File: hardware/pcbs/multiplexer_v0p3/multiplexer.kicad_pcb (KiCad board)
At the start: 2 copper layers, 82.6 x 88.9 mm, 22 parts, among them K1 CONN_3, M1 VAL**, M2 VAL**, M3 VAL**, P1 CONN_5X2, P2 CONN_5X2, P3 CONN_2, P4 CONN_2, P5 CONN_5X2, U1 ADG44X, U2 ADG44X, U3 ADG44X, U4 ADG44X

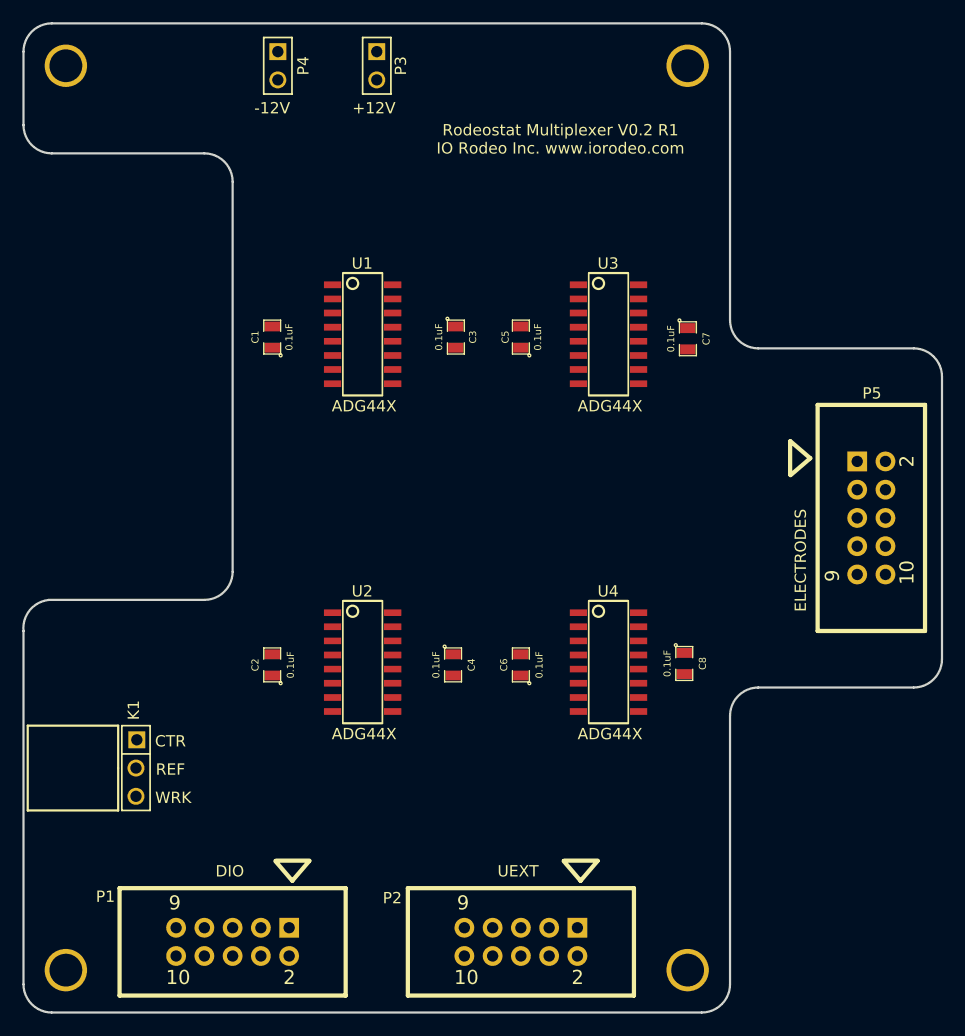
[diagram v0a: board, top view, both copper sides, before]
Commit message: Worked on layout of v0.3 multiplexer design.
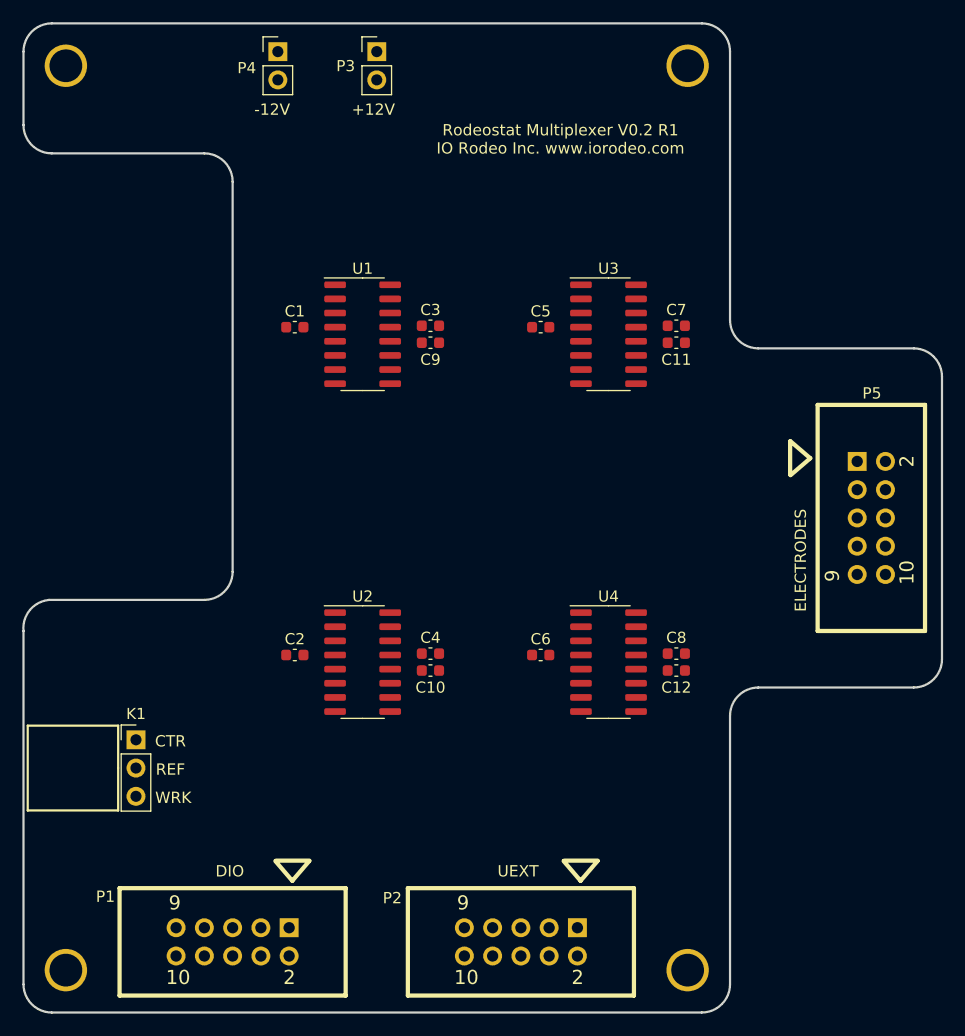
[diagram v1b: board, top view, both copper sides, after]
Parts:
- added C10: 0.1uF, Capacitor_SMD:C_0603_1608Metric, F.Cu at (112.8, 134.4)
- added C11: 0.1uF, Capacitor_SMD:C_0603_1608Metric, F.Cu at (134.9, 104.9)
- added C12: 0.1uF, Capacitor_SMD:C_0603_1608Metric, F.Cu at (134.9, 134.4)
- added C9: 0.1uF, Capacitor_SMD:C_0603_1608Metric, F.Cu at (112.8, 104.9)
- C1, C2, C3, C4, C5, C6, C7, C8: footprint SM0805 -> Capacitor_SMD:C_0603_1608Metric
- K1: footprint PIN_ARRAY_3X1 -> Connector_PinHeader_2.54mm:PinHeader_1x03_P2.54mm_Vertical
- P1, P2, P5: footprint 5X2_SHRD_HEADER -> 5x2_shrd_header:5X2_SHRD_HEADER
- P3, P4: footprint PIN_ARRAY_2X1 -> Connector_PinHeader_2.54mm:PinHeader_1x02_P2.54mm_Vertical
- U1, U2, U3, U4: value ADG44X -> DG411xY; footprint 16-SOIC-0154 -> Package_SO:SOIC-16_3.9x9.9mm_P1.27mm
- moved K1 2.54 mm to (86.3, 140.6), turned to 0 degrees
- moved C3 2.50 mm to (112.8, 103.4), turned to 0 degrees
- moved C4 2.27 mm to (112.8, 132.8), turned to 0 degrees
- moved C1 2.22 mm to (100.6, 103.5), turned to 0 degrees
- moved C2 2.22 mm to (100.6, 133.0), turned to 0 degrees
- moved C5 1.99 mm to (122.7, 103.5), turned to 0 degrees
- moved C6 1.99 mm to (122.7, 133.0), turned to 0 degrees
- moved C7 1.56 mm to (134.9, 103.4), turned to 0 degrees
- moved P3 1.27 mm to (108.0, 78.7), turned to 0 degrees
- moved P4 1.27 mm to (99.1, 78.7), turned to 0 degrees
- moved C8 1.14 mm to (134.9, 132.8), turned to 0 degrees
- turned U1 to 0 degrees
- turned U2 to 0 degrees
- turned U3 to 0 degrees
- turned U4 to 0 degrees
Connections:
- net /+12V renamed /+15V
- net /-12V renamed /-15V
- P1 pad 1: (no net) -> /3V3
- P2 pad 1: (no net) -> Net-(P2-Pad1)
- P2 pad 2: (no net) -> Net-(P2-Pad2)
- U1 pad 12: (no net) -> /3V3
- U1 pad 15: /WRK_2 -> /WRK_4
- U1 pad 16: /D25 -> /D27
- U1 pad 6: /WRK -> /WRK_2
- U1 pad 7: /WRK_4 -> /WRK
- U1 pad 8: /D27 -> /D25
- U2 pad 12: (no net) -> /3V3
- U2 pad 15: /WRK_2 -> /WRK_4
- U2 pad 16: /D29 -> /D31
- U2 pad 6: /GND -> /WRK_2
- U2 pad 7: /WRK_4 -> /GND
- U2 pad 8: /D31 -> /D29
- U3 pad 12: (no net) -> /3V3
- U3 pad 15: /WRK_5 -> /WRK_7
- U3 pad 16: /D4 -> /D18
- U3 pad 6: /WRK -> /WRK_5
- U3 pad 7: /WRK_7 -> /WRK
- U3 pad 8: /D18 -> /D4
- U4 pad 12: (no net) -> /3V3
- U4 pad 15: /WRK_5 -> /WRK_7
- U4 pad 16: /D11 -> /D10
- U4 pad 6: /GND -> /WRK_5
- U4 pad 7: /WRK_7 -> /GND
- U4 pad 8: /D10 -> /D11

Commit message: Added preliminary routing of v0.3 mulitplexer design.
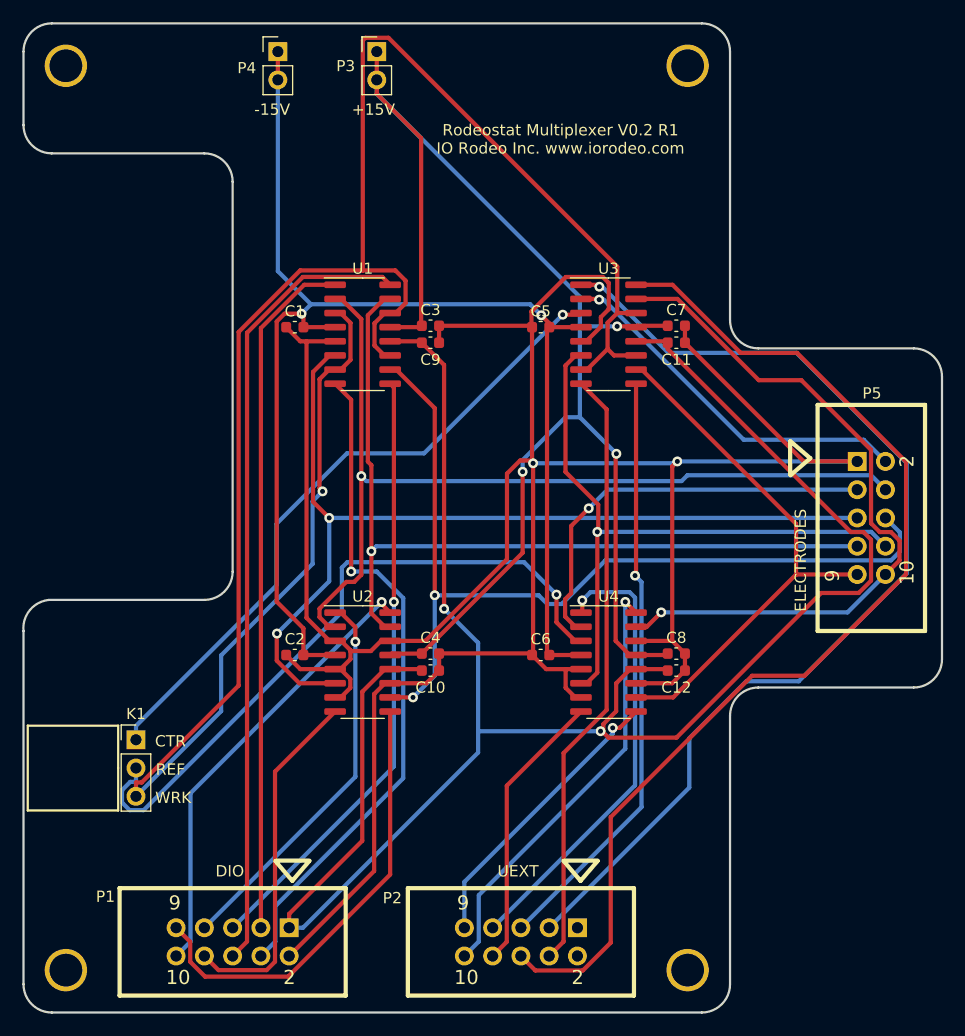
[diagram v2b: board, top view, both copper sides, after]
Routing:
- net /GND: track 0.00 -> 259.7 mm, vias 0 -> 2
- net /WRK: track 0.00 -> 193.6 mm, vias 0 -> 1
- net /3V3: track 0.00 -> 179.5 mm, vias 0 -> 2
- net /+15V: track 0.00 -> 132.6 mm, vias 0 -> 3
- net /-15V: track 0.00 -> 123.4 mm, vias 0 -> 2
- net /D18: track 0.00 -> 97.5 mm
- net /D3: track 0.00 -> 93.7 mm, vias 0 -> 1
- net /WRK_2: track 0.00 -> 84.6 mm, vias 0 -> 2
- net /WRK_3: track 0.00 -> 81.9 mm, vias 0 -> 2
- net /WRK_1: track 0.00 -> 81.7 mm, vias 0 -> 1
- net /WRK_4: track 0.00 -> 75.6 mm, vias 0 -> 1
- net /D27: track 0.00 -> 71.8 mm
- net /WRK_7: track 0.00 -> 64.5 mm, vias 0 -> 1
- net /D24: track 0.00 -> 62.2 mm
- net /REF: track 0.00 -> 61.4 mm, vias 0 -> 1
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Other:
- board text added: "+15V"
- board text added: "-15V"
- board text removed: "+12V"
- board text removed: "-12V"

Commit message: Added fab files.
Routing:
- net /WRK: track 193.6 -> 163.1 mm, vias 1 -> 3
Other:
- board text added: "Rodeostat Multiplexer V0.3 R1 IO Rodeo Inc. www.iorodeo.com"
- board text removed: "Rodeostat Multiplexer V0.2 R1 IO Rodeo Inc. www.iorodeo.com"
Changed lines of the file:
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@@
     (thickness 1.6)
     (drawings 42)
-    (tracks 451)
+    (tracks 455)
     (zones 0)
     (modules 26)
@@
     (visible_elements FFFFFFBF)
     (pcbplotparams
-      (layerselection 0x00030_ffffffff)
+      (layerselection 0x010fc_ffffffff)
       (usegerberextensions true)
       (usegerberattributes true)
@@
       (drillshape 0)
       (scaleselection 1)
-      (outputdirectory "gerber_v0p2/"))
+      (outputdirectory "gerber_v0p3/"))
   )
   (net 0 "")
@@
   (gr_arc (start 142.24 138.43) (end 139.7 138.43) (angle 90) (layer Edge.Cuts) (width 0.2))
   (gr_arc (start 142.24 102.87) (end 142.24 105.41) (angle 90) (layer Edge.Cuts) (width 0.2))
-  (gr_text "Rodeostat Multiplexer V0.2 R1\nIO Rodeo Inc. www.iorodeo.com" (at 124.46 86.614) (layer F.SilkS)
+  (gr_text "Rodeostat Multiplexer V0.3 R1\nIO Rodeo Inc. www.iorodeo.com" (at 125.9078 86.8172) (layer F.SilkS)
     (effects (font (size 1.016 1.016) (thickness 0.2032)))
   )
@@
   (segment (start 129.2718 106.045) (end 131.253 106.045) (width 0.381) (layer F.Cu) (net 22))
   (segment (start 129.5643 102.235) (end 129.5643 98.0552) (width 0.381) (layer F.Cu) (net 22))
-  (segment (start 129.5643 98.0552) (end 109.005 77.4959) (width 0.381) (layer F.Cu) (net 22))
-  (segment (start 109.005 77.4959) (end 106.93 77.4959) (width 0.381) (layer F.Cu) (net 22))
-  (segment (start 106.93 77.4959) (end 106.6954 77.7305) (width 0.381) (layer F.Cu) (net 22))
-  (segment (start 106.6954 77.7305) (end 106.6954 98.4035) (width 0.381) (layer F.Cu) (net 22))
   (segment (start 131.253 102.235) (end 129.5643 102.235) (width 0.381) (layer F.Cu) (net 22))
   (segment (start 104.205 107.315) (end 104.7187 107.315) (width 0.381) (layer F.Cu) (net 22))
@@
   (segment (start 108.6346 106.045) (end 109.155 106.045) (width 0.381) (layer F.Cu) (net 22))
   (via (at 103.077 118.2616) (size 0.889) (layers F.Cu B.Cu) (net 22))
+  (via (at 110.744 97.2312) (size 0.889) (drill 0.635) (layers F.Cu B.Cu) (net 22))
+  (segment (start 109.6172 98.358) (end 110.744 97.2312) (width 0.381) (layer F.Cu) (net 22))
+  (segment (start 109.6172 98.4035) (end 109.6172 98.358) (width 0.381) (layer F.Cu) (net 22))
+  (segment (start 111.76 96.2152) (end 120.3452 96.2152) (width 0.381) (layer B.Cu) (net 22))
+  (via (at 120.3452 96.2152) (size 0.889) (drill 0.635) (layers F.Cu B.Cu) (net 22))
+  (segment (start 110.744 97.2312) (end 111.76 96.2152) (width 0.381) (layer B.Cu) (net 22))
+  (segment (start 127.7243 96.2152) (end 129.5643 98.0552) (width 0.381) (layer F.Cu) (net 22))
+  (segment (start 120.3452 96.2152) (end 127.7243 96.2152) (width 0.381) (layer F.Cu) (net 22))
   (segment (start 106.5627 116.8923) (end 107.0075 117.3371) (width 0.381) (layer B.Cu) (net 23))
   (segment (start 107.0075 117.3371) (end 135.3473 117.3371) (width 0.381) (layer B.Cu) (net 23))
